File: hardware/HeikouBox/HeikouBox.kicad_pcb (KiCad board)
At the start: 2 copper layers, 100 x 100 mm, 189 parts, among them J101 5V, J201 Conn_02x05_Odd_Even, J202 Conn_02x08_Odd_Even, J301 DB15_Female_HighDensity_Mount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, J302 AudioJack3_SwitchTR, J501 Micro_SD_Card_TFP09-2-12B, J503 PS/2, Q301 MMBT3904, Q302 MMBT3904, Q303 MMBT3904, Q304 MMBT3904, Q305 MMBT3904, Q306 MMBT3904, Q307 MMBT3904, Q502 BSS138, Q503 BSS138, SW501 Left, SW502 Right, SW503 Up, SW504 Down, U101 LD1117S33TR, U102 LD1117S25TR, U103 LD1117S12TR, U201 HeikouBox-Core, U202 74HCU04, U401 K4S281632-UC60, U501 STM32-BluePill-Socket, Y201 14.31818MHz, Y202 28.37516MHz

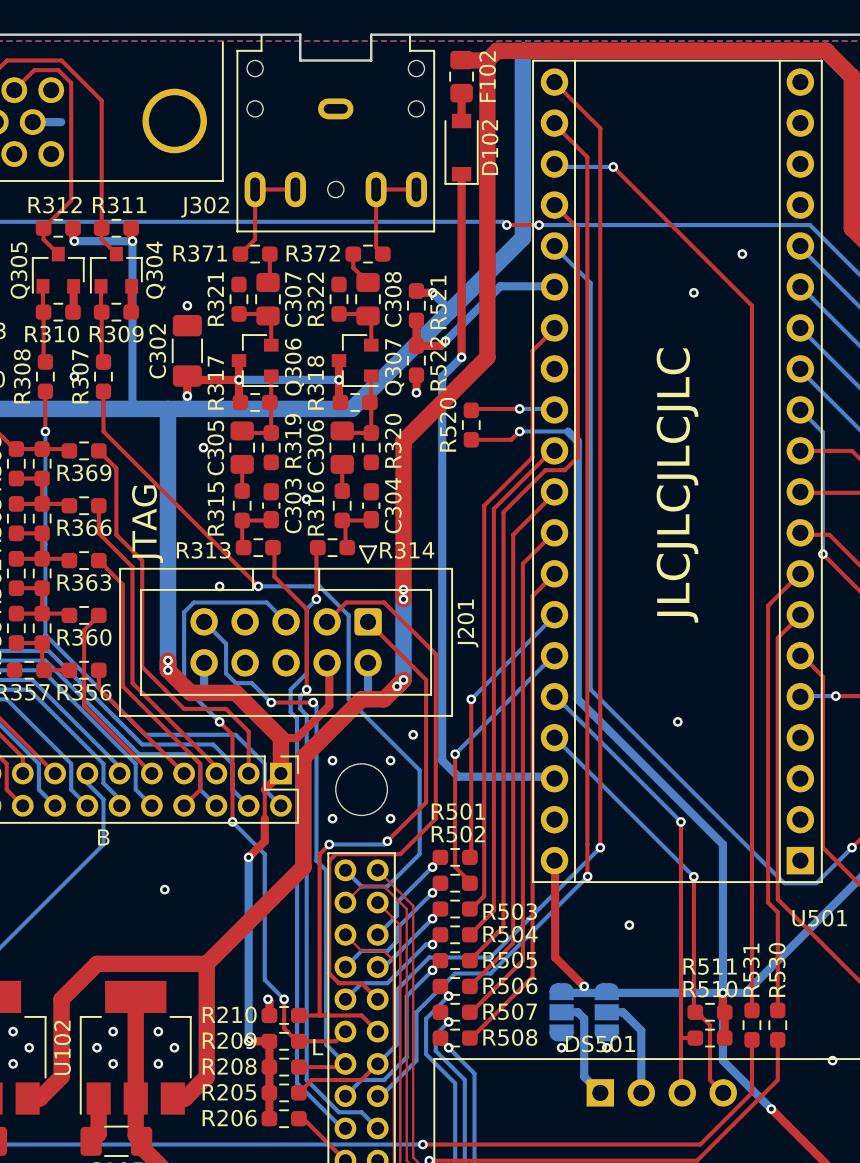
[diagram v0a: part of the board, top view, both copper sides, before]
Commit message: Fix dumb routing around JTAG
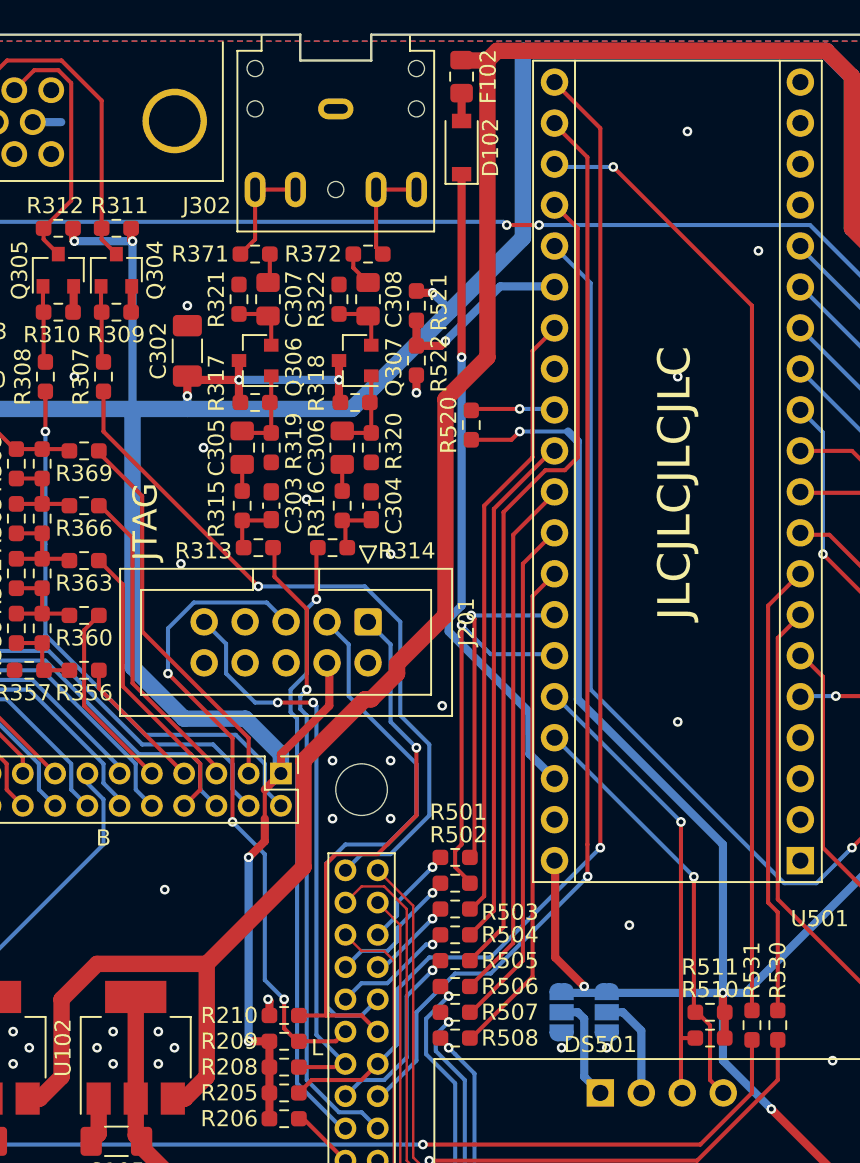
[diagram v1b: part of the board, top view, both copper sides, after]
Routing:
- net /part5-hub/MDB1_TX_R: track 17.1 -> 23.1 mm
- net /part1-power/VUSB: track 44.3 -> 40.5 mm
- net /part2-core/jtag_TDO: track 37.1 -> 33.8 mm
- net /part5-hub/MDB0_RX_R: track 17.2 -> 20.4 mm
- net /part1-power/GND: track 77.9 -> 75.0 mm, vias 107 -> 109
- net /part1-power/3V3: track 533.3 -> 535.2 mm, vias 28 -> 26
- net /part1-power/5V: track 213.0 -> 211.2 mm, vias 7 -> 3
- net /part3-av/BLU4: track 25.4 -> 23.8 mm
- net /part2-core/jtag_TCK: track 35.9 -> 34.8 mm, vias 2 -> 1
- net /part2-core/jtag_TMS: track 39.8 -> 40.6 mm

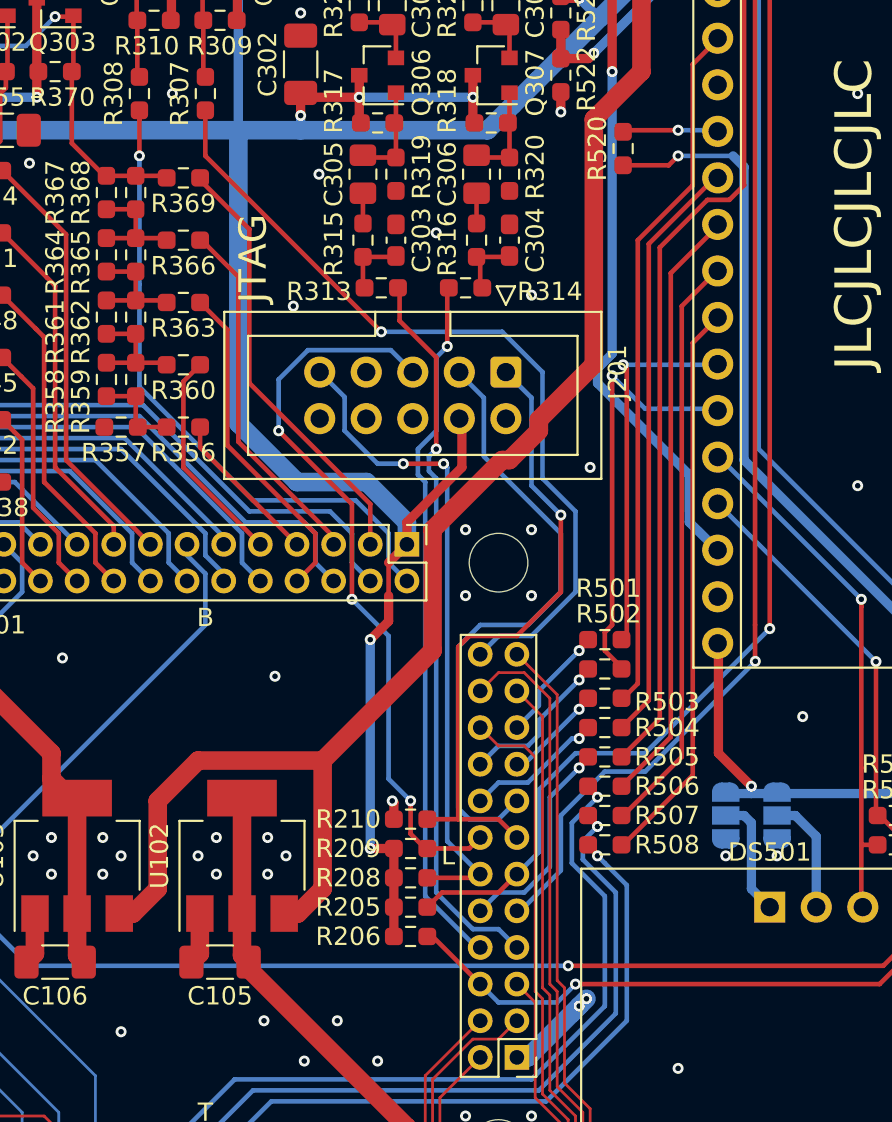
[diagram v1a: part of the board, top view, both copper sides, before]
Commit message: Run 1.2v vreg from 3.3v to spread power
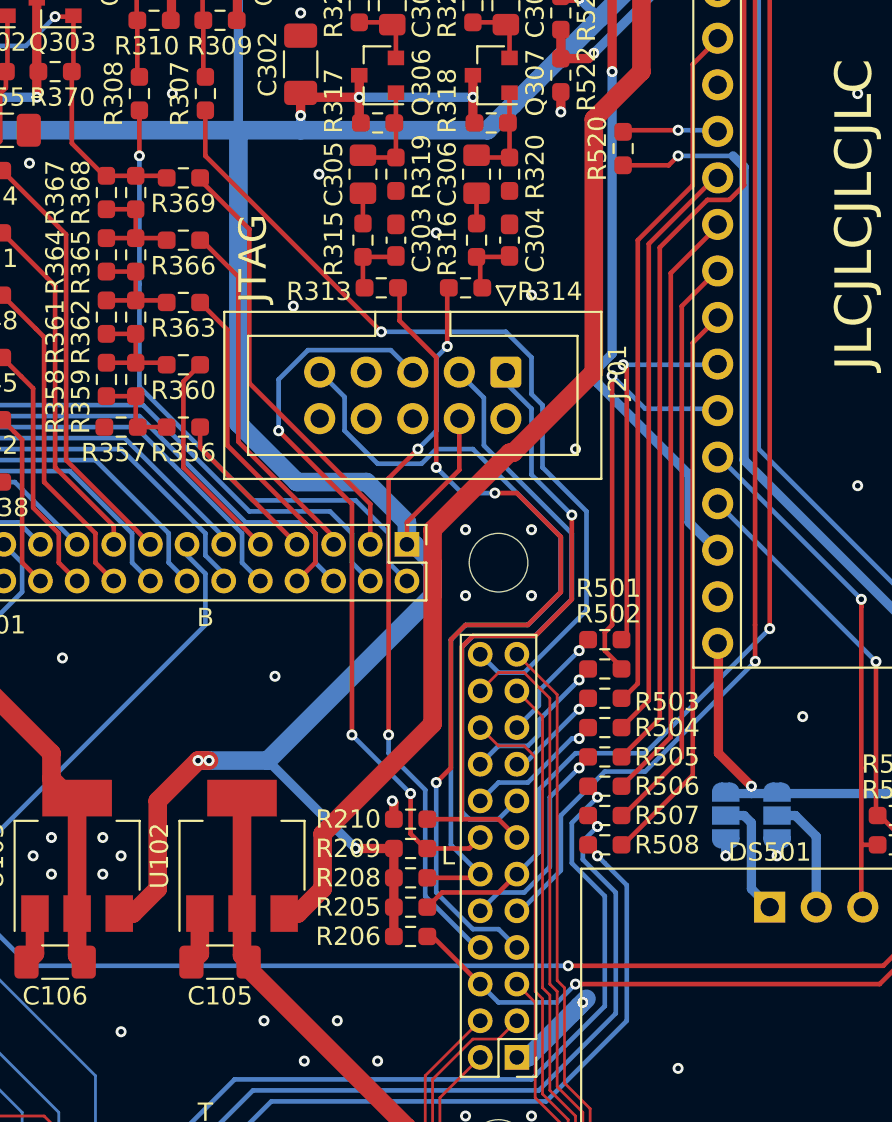
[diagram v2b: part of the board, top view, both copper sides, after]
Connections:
- U103 pad 3: /part1-power/5V -> /part1-power/3V3
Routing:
- net /part1-power/3V3: track 535.2 -> 556.6 mm, vias 26 -> 27
- net /part1-power/5V: track 211.2 -> 193.8 mm
- net /part3-av/LSIGMA: track 39.8 -> 48.9 mm, vias 1 -> 3
- net /part2-core/jtag_TDI: track 36.1 -> 45.1 mm, vias 2 -> 0
- net /part3-av/NHSYNC: track 45.1 -> 47.5 mm
- net /part1-power/GND: track 75.0 -> 76.8 mm, vias 109 -> 102
- net /part3-av/RSIGMA: track 38.2 -> 39.6 mm, vias 1 -> 3
- net /part2-core/jtag_TCK: track 34.8 -> 35.7 mm
- net /part2-core/jtag_TDO: track 33.8 -> 34.6 mm

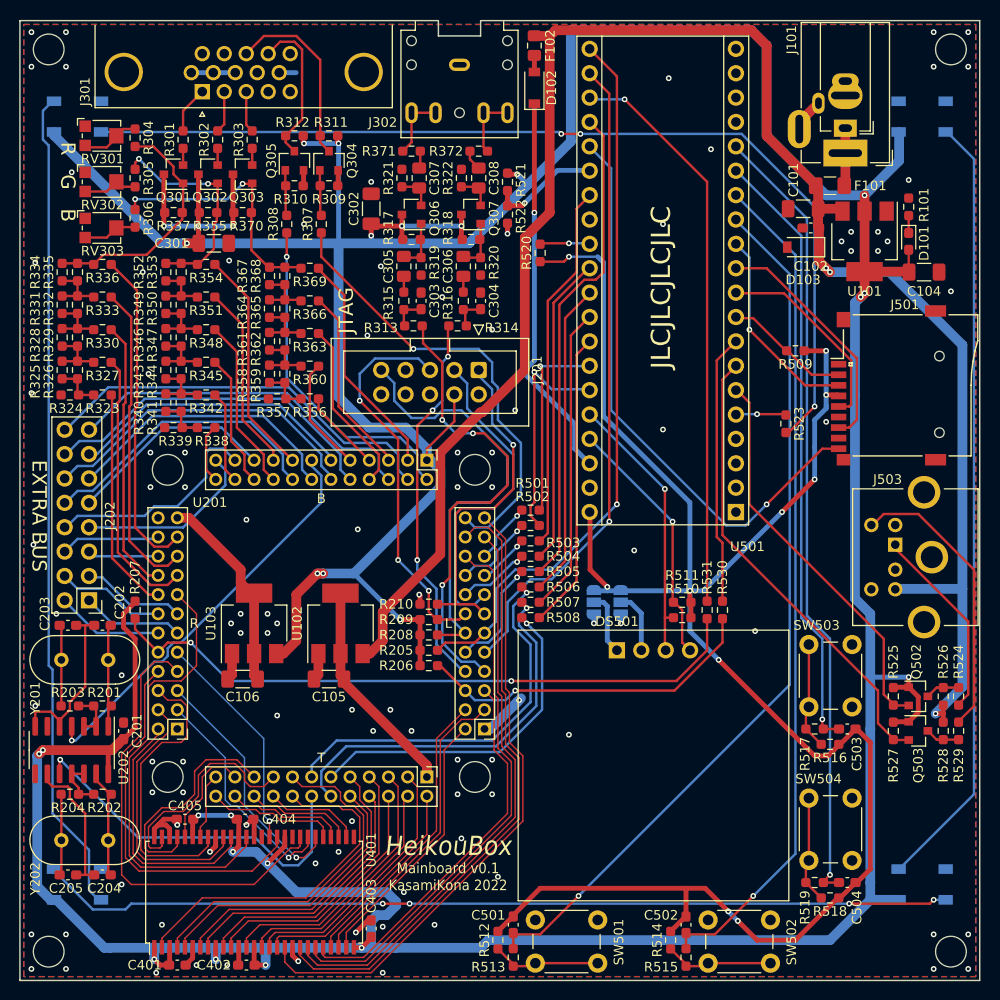
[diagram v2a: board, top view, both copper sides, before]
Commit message: Add 1ohm series resistors to regulator output caps
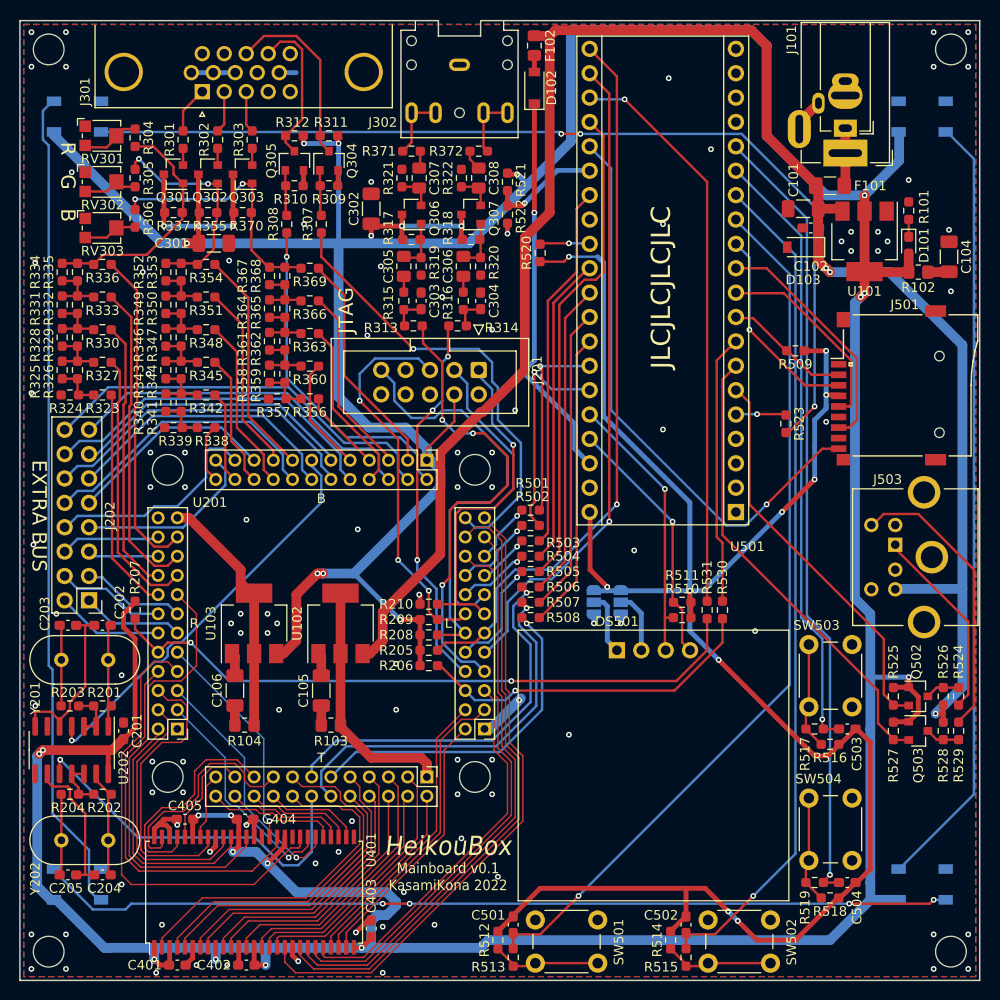
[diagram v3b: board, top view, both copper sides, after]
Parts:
- added R102: 1R, Resistor_SMD:R_0805_2012Metric_Pad1.20x1.40mm_HandSolder, F.Cu at (108.4, 46.6)
- added R103: 1R, Resistor_SMD:R_0805_2012Metric_Pad1.20x1.40mm_HandSolder, F.Cu at (47.2, 93.8)
- added R104: 1R, Resistor_SMD:R_0805_2012Metric_Pad1.20x1.40mm_HandSolder, F.Cu at (38.2, 93.8)
- moved C104 3.05 mm to (111.6, 45.0), turned to 90 degrees
- moved C105 1.44 mm to (46.2, 90.2), turned to 90 degrees
- moved C106 1.44 mm to (37.2, 90.2), turned to 90 degrees
- moved R101 0.40 mm to (107.4, 40.2)
- moved D101 0.40 mm to (107.4, 43.8)
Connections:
- C104 pad 1: /part1-power/3V3 -> Net-(C104-Pad1)
- C105 pad 1: /part1-power/2V5 -> Net-(C105-Pad1)
- C106 pad 1: /part1-power/1V2 -> Net-(C106-Pad1)
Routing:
- net /part1-power/1V2: track 21.2 -> 25.8 mm
- net /part1-power/2V5: track 22.9 -> 25.9 mm
- net Net-(C104-Pad1): track 0.00 -> 2.22 mm
- net Net-(C106-Pad1): track 0.00 -> 2.04 mm
- net Net-(C105-Pad1): track 0.00 -> 2.04 mm
- net /part1-power/GND: track 76.8 -> 75.9 mm, vias 102 -> 101

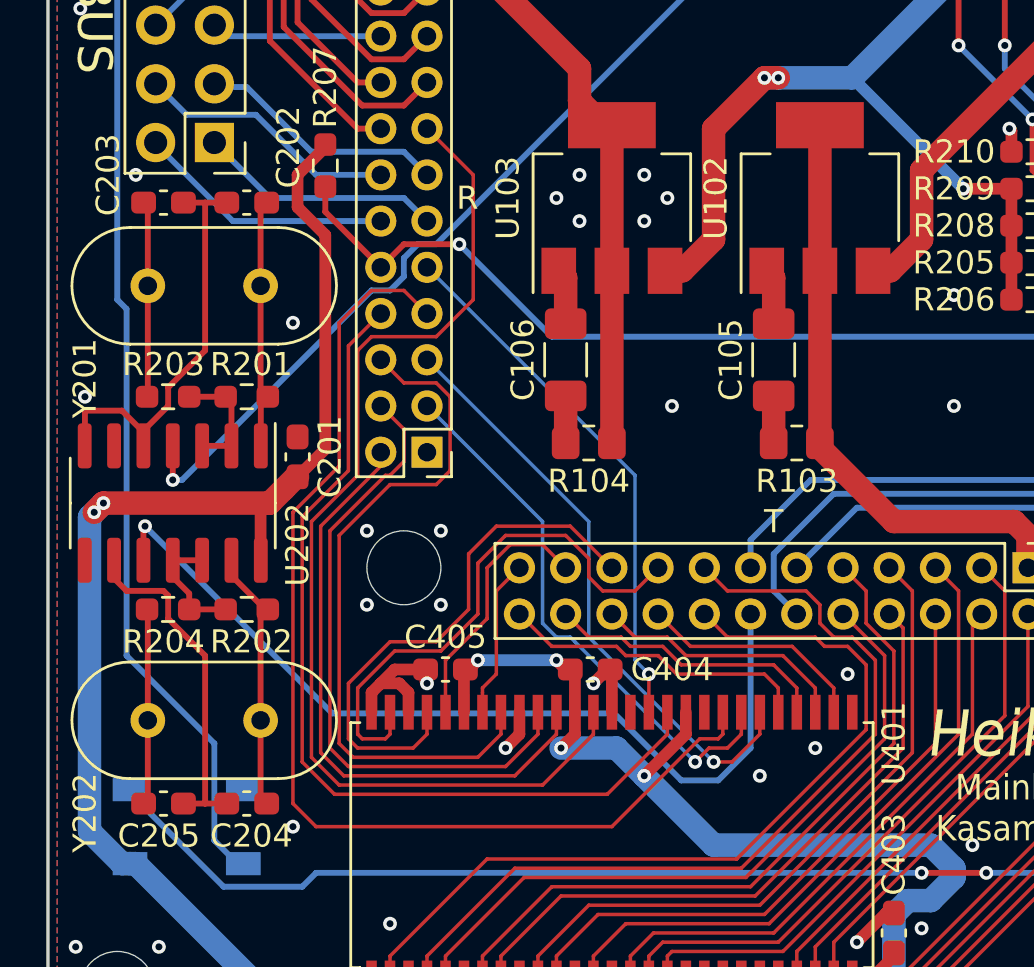
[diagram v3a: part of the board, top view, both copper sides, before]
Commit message: Cleanup, add regulator input caps
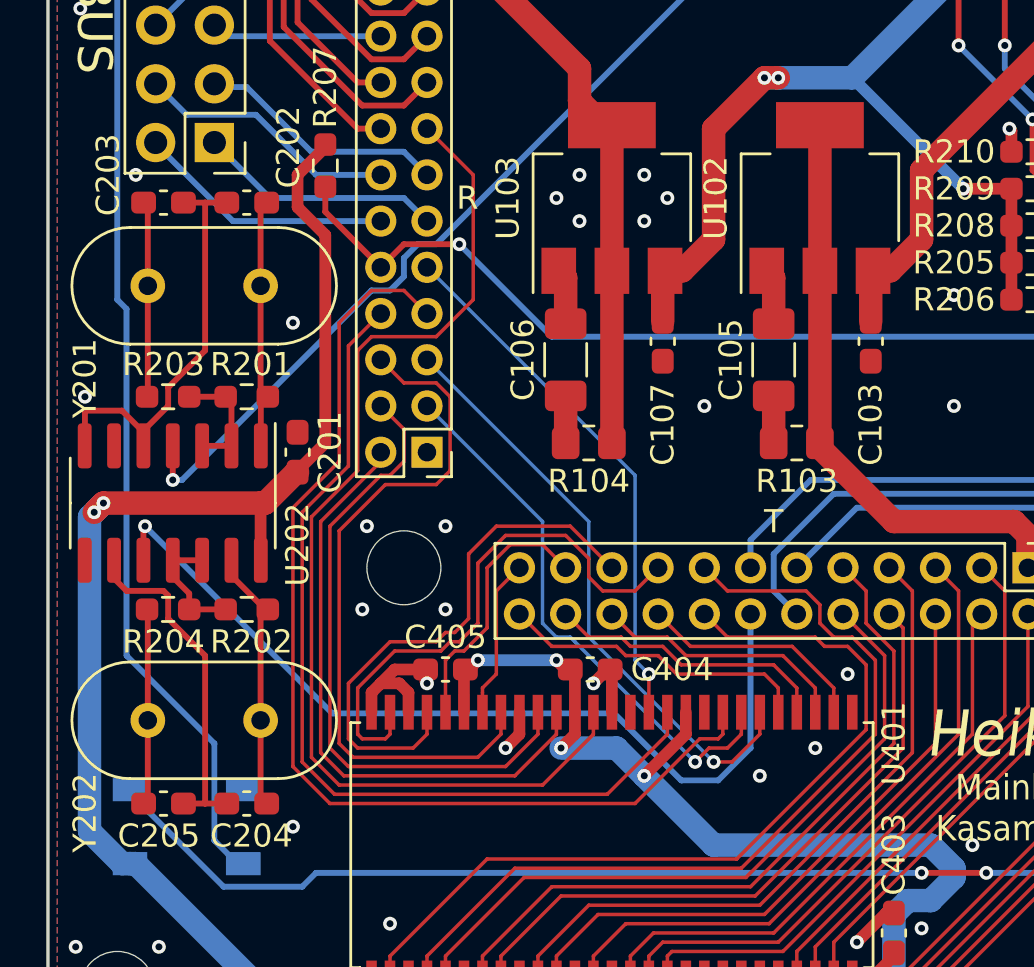
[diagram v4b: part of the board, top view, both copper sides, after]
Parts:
- added C103: 100n, Capacitor_SMD:C_0603_1608Metric_Pad1.08x0.95mm_HandSolder, F.Cu at (50.4, 89.4)
- added C107: 100n, Capacitor_SMD:C_0603_1608Metric_Pad1.08x0.95mm_HandSolder, F.Cu at (41.4, 89.4)
- moved C201 0.20 mm to (25.6, 94.2)
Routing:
- net /part1-power/5V: track 193.8 -> 196.0 mm
- net /part1-power/3V3: track 556.1 -> 558.1 mm
- net /part4-memory/A11: track 48.0 -> 46.3 mm
